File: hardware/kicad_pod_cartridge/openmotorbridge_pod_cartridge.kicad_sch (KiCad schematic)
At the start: 31 parts, among them Q1 AO3400A, Q2 AO3400A, Q3 AO3400A, Q4 AO3400A, U1 ESP32-C6-MINI-1U, U3 ES8388, U4 TS5A3159DBVR

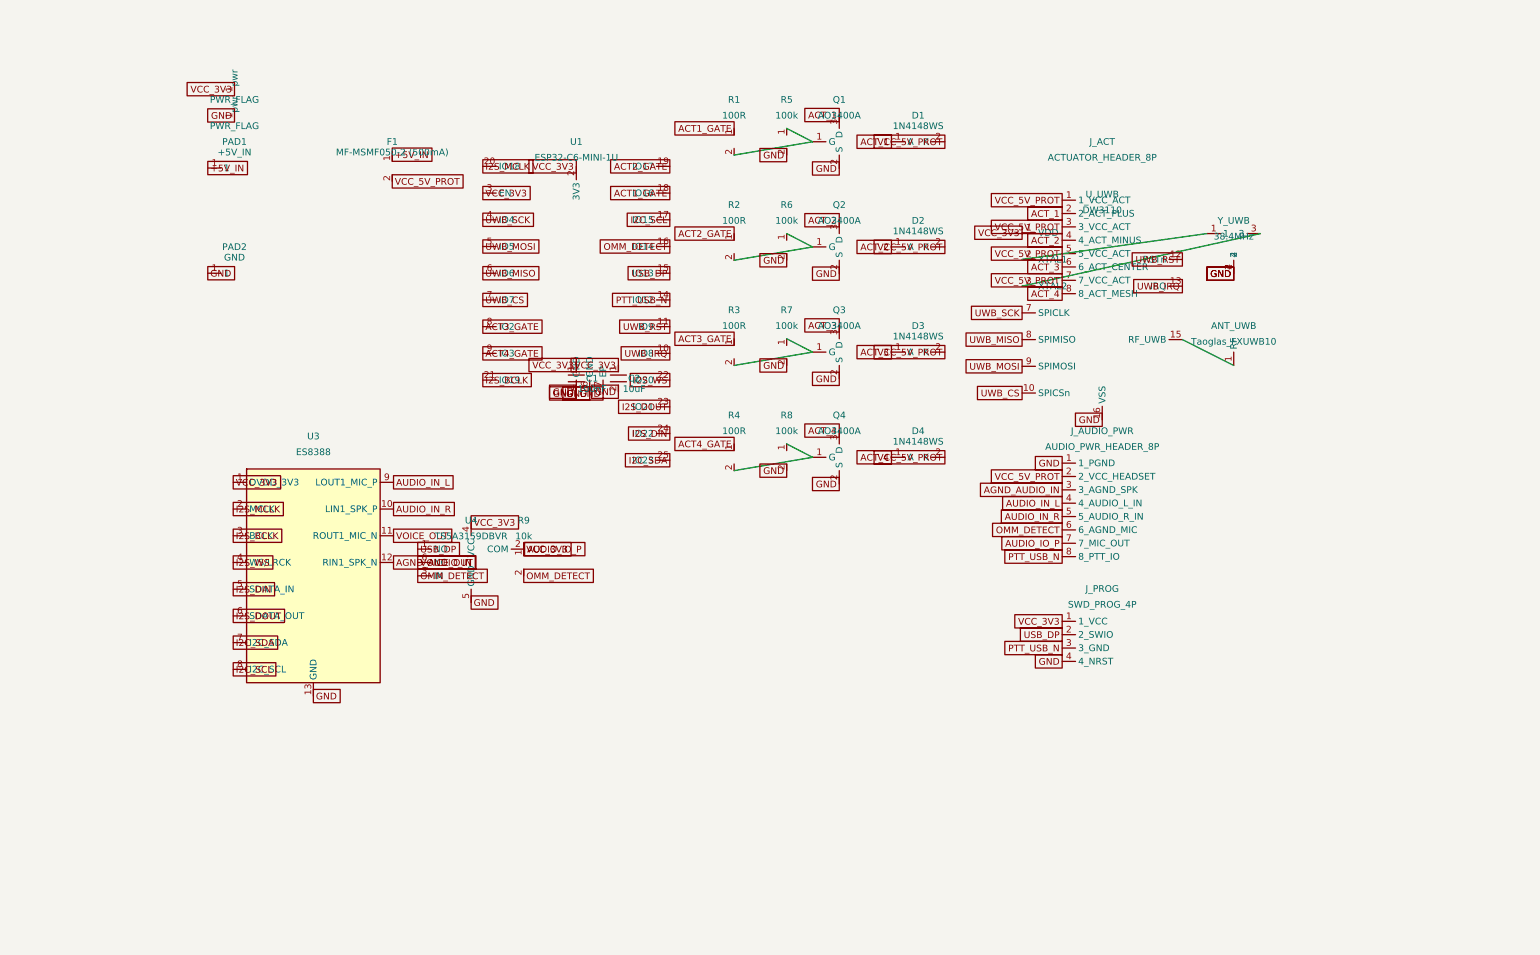
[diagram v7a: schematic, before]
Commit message: fix(cartridge): complete 100% prefab-gate schematic parity and document audio switching in 04b & 07
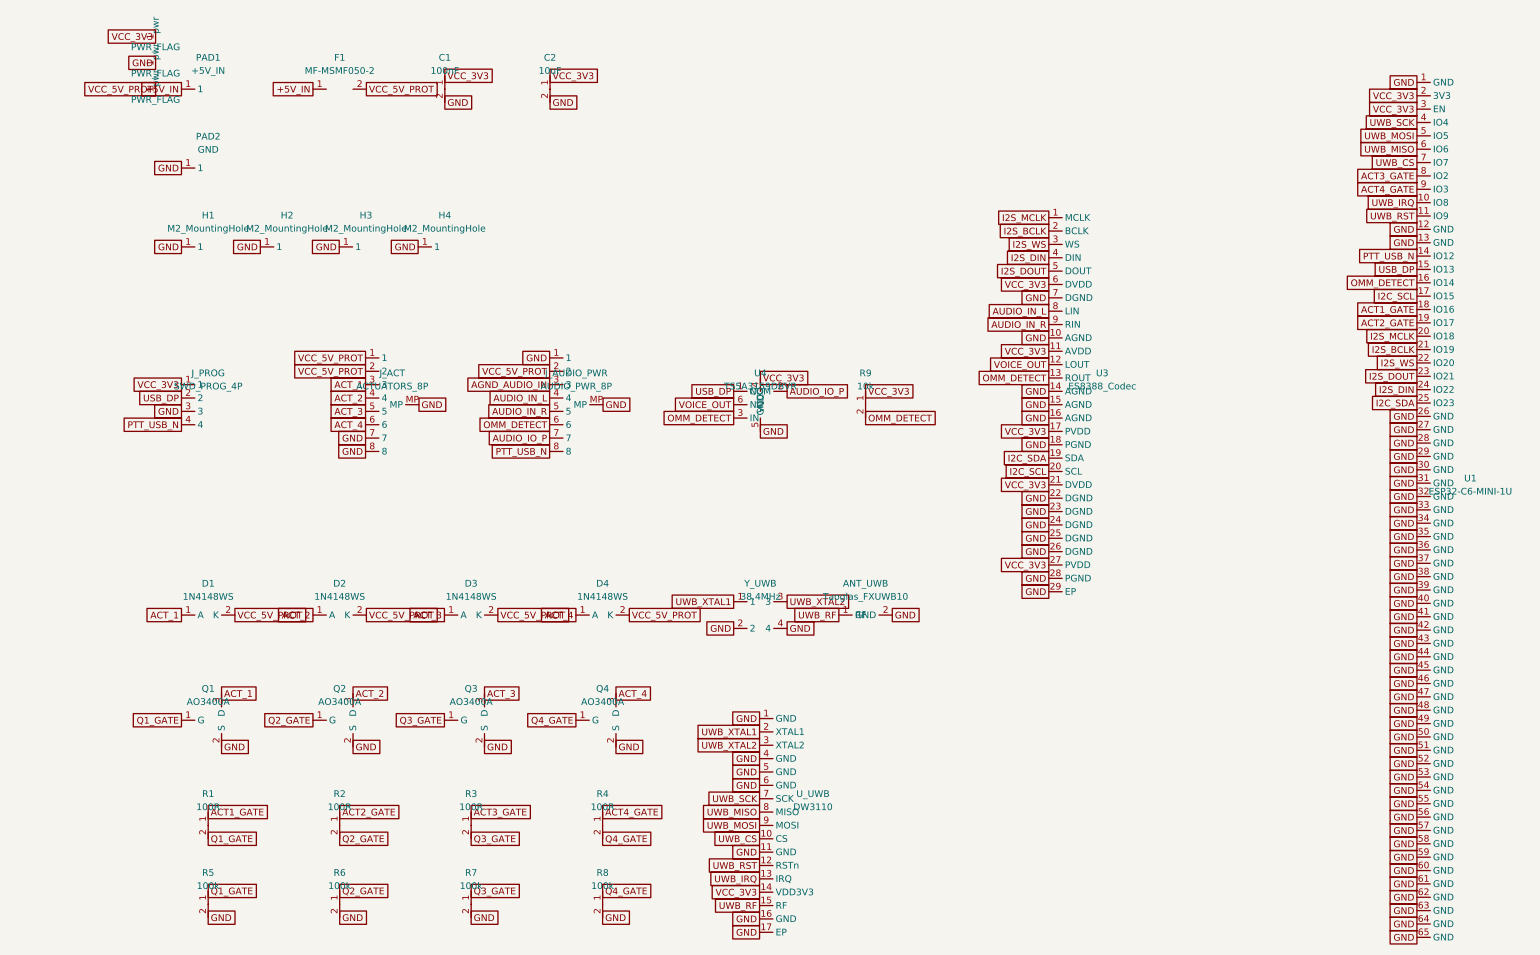
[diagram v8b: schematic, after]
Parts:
- removed ANT_UWB: Taoglas_FXUWB10, Connector_Coaxial:U.FL_Hirose_U.FL-R-SMT-1_Vertical, symbol Device:Antenna
- removed J_ACT: ACTUATOR_HEADER_8P, Connector_JST:JST_SH_SM08B-SRSS-TB_1x08-1MP_P1.00mm_Horizontal, symbol Connector:Conn_01x08
- removed J_AUDIO_PWR: AUDIO_PWR_HEADER_8P, Connector_JST:JST_SH_SM08B-SRSS-TB_1x08-1MP_P1.00mm_Horizontal, symbol Connector:Conn_01x08_Audio
- removed J_PROG: SWD_PROG_4P, Connector_PinHeader_1.27mm:PinHeader_1x04_P1.27mm_Vertical_SMD_Pin1Left, symbol Connector:Conn_01x04_SWD
- removed U3: ES8388, Package_DFN_QFN:QFN-28-1EP_4x4mm_P0.4mm_EP2.4x2.4mm, symbol Audio:ES8388
- removed Y_UWB: 38.4MHz, Crystal:Crystal_SMD_2016-4Pin_2.0x1.6mm, symbol Device:Crystal_Small
- added ANT_UWB: Taoglas_FXUWB10, Connector_Coaxial:U.FL_Hirose_U.FL-R-SMT-1_Vertical, symbol Connector_Coaxial:U.FL
- added H1, H2, H3, H4: M2_MountingHole, MountingHole:MountingHole_2.2mm_M2_Pad, symbol Mechanical:MountingHole_Pad
- added J_ACT: ACTUATORS_8P, Connector_JST:JST_SH_SM08B-SRSS-TB_1x08-1MP_P1.00mm_Horizontal, symbol Connector_JST:JST_SH_SM08B_Shielded
- added J_AUDIO_PWR: AUDIO_PWR_8P, Connector_JST:JST_SH_SM08B-SRSS-TB_1x08-1MP_P1.00mm_Horizontal, symbol Connector_JST:JST_SH_SM08B_Shielded
- added J_PROG: SWD_PROG_4P, Connector_PinHeader_1.27mm:PinHeader_1x04_P1.27mm_Vertical_SMD_Pin1Left, symbol Connector_PinHeader:PinHeader_1x04
- added U3: ES8388_Codec, Package_DFN_QFN:QFN-28-1EP_4x4mm_P0.4mm_EP2.4x2.4mm, symbol Audio:ES8388_Codec
- added Y_UWB: 38.4MHz, Crystal:Crystal_SMD_2016-4Pin_2.0x1.6mm, symbol Device:Crystal_4Pin
- C1: LCSC C14663 -> (none)
- C2: LCSC C15850 -> (none)
- D1, D2, D3, D4: LCSC C81598 -> (none)
- F1: value MF-MSMF050-2 (500mA) -> MF-MSMF050-2; LCSC C20739 -> (none)
- PAD1, PAD2: footprint TestPoint:TestPoint_Pad_D2.0mm_SMD -> TestPoint:TestPoint_Pad_D3.0mm_OD3.5mm
- Q1, Q2, Q3, Q4: LCSC C20917 -> (none)
- R1, R2, R3, R4: LCSC C22775 -> (none)
- R5, R6, R7, R8: LCSC C25803 -> (none)
- R9: LCSC C25804 -> (none)
- U1: footprint RF_Module:ESP32-C6-MINI-1U -> RF_Module:ESP32-S2-MINI-1U; LCSC C5287747 -> (none)
- U4: LCSC C12933 -> (none)
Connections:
- net ACT_1: now also J_ACT.3
- net ACT_2: now also J_ACT.4
- net ACT_3: now also J_ACT.5
- net ACT_4: now also J_ACT.6
- net AGND_AUDIO_IN: now also J_AUDIO_PWR.3
- net AUDIO_IN_L: now also J_AUDIO_PWR.4, U3.8 (LIN)
- net AUDIO_IN_R: now also J_AUDIO_PWR.5, U3.9 (RIN)
- net AUDIO_IO_P: now also J_AUDIO_PWR.7
- net GND: now also U1.12 (GND), U1.13 (GND), U1.28 (GND), U1.29 (GND), U1.30 (GND), U1.31 (GND), U1.32 (GND), U1.33 (GND), U1.34 (GND), U1.35 (GND), U1.36 (GND), U1.37 (GND), U1.38 (GND), U1.39 (GND), U1.40 (GND), U1.41 (GND), U1.42 (GND), U1.43 (GND), U1.44 (GND), U1.45 (GND), U1.46 (GND), U1.47 (GND), U1.48 (GND), U1.49 (GND), U1.50 (GND), U1.51 (GND), U1.52 (GND), U1.53 (GND), U1.54 (GND), U1.55 (GND), U1.56 (GND), U1.57 (GND), U1.58 (GND), U1.59 (GND), U1.60 (GND), U1.61 (GND), U1.62 (GND), U1.63 (GND), U1.64 (GND), U1.65 (GND), U_UWB.1 (GND), U_UWB.11 (GND), U_UWB.17 (EP), U_UWB.4 (GND), U_UWB.5 (GND), U_UWB.6 (GND), ANT_UWB.2 (GND), H1.1, H2.1, H3.1, H4.1, J_ACT.7, J_ACT.8, J_ACT.MP, J_AUDIO_PWR.1, J_AUDIO_PWR.MP, J_PROG.3, U3.10 (AGND), U3.14 (AGND), U3.15 (AGND), U3.16 (AGND), U3.18 (PGND), U3.22 (DGND), U3.23 (DGND), U3.24 (DGND), U3.25 (DGND), U3.26 (DGND), U3.28 (PGND), U3.29 (EP), U3.7 (DGND), Y_UWB.2, Y_UWB.4
- net I2C_SCL: now also U3.20 (SCL)
- net I2C_SDA: now also U3.19 (SDA)
- net I2S_BCLK: now also U3.2 (BCLK)
- net I2S_DIN: now also U3.4 (DIN)
- net I2S_DOUT: now also U3.5 (DOUT)
- net I2S_MCLK: now also U3.1 (MCLK)
- net I2S_WS: now also U3.3 (WS)
- net OMM_DETECT: now also J_AUDIO_PWR.6, U3.13 (ROUT)
- net PTT_USB_N: now also J_AUDIO_PWR.8, J_PROG.4
- net USB_DP: now also J_PROG.2
- net VCC_3V3: now also U_UWB.14 (VDD3V3), J_PROG.1, U3.11 (AVDD), U3.17 (PVDD), U3.21 (DVDD), U3.27 (PVDD), U3.6 (DVDD); no longer U_UWB.1 (VDD)
- net VCC_5V_PROT: now also J_ACT.1, J_ACT.2, J_AUDIO_PWR.2
- net VOICE_OUT: now also U3.12 (LOUT)
- net Q1_GATE: now reaches Q1.1 (G), R1.2, R5.1
- net Q2_GATE: now reaches Q2.1 (G), R2.2, R6.1
- net Q3_GATE: now reaches Q3.1 (G), R3.2, R7.1
- net Q4_GATE: now reaches Q4.1 (G), R4.2, R8.1
- net UWB_RF: now reaches U_UWB.15 (RF)
- net UWB_RF: now also ANT_UWB.1 (RF)
- net UWB_XTAL1: now reaches U_UWB.2 (XTAL1)
- net UWB_XTAL1: now also Y_UWB.1
- net UWB_XTAL2: now reaches U_UWB.3 (XTAL2)
- net UWB_XTAL2: now also Y_UWB.3
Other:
- title: OpenMotorBridge v9.6 - Smart Modular Cartridge Rev 3.0 (with ES8388 Audio Codec) -> OpenMotorBridge PCBA 03 - Universal Smart Modular Cartridge Rev 3.0
